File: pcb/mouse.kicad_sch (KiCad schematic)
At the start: 42 parts, among them J1 Conn_02x03_Counter_Clockwise, SW1 SW_MEC_5E, SW2 SW_DPDT_x2, SW3 SW_DPDT_x2, SW4 RotaryEncoder, SW5 SW_DPDT_x2, SW6 SW_DPDT_x2, U1 STM32F042K6Tx, U2 pmw3360-t2qu

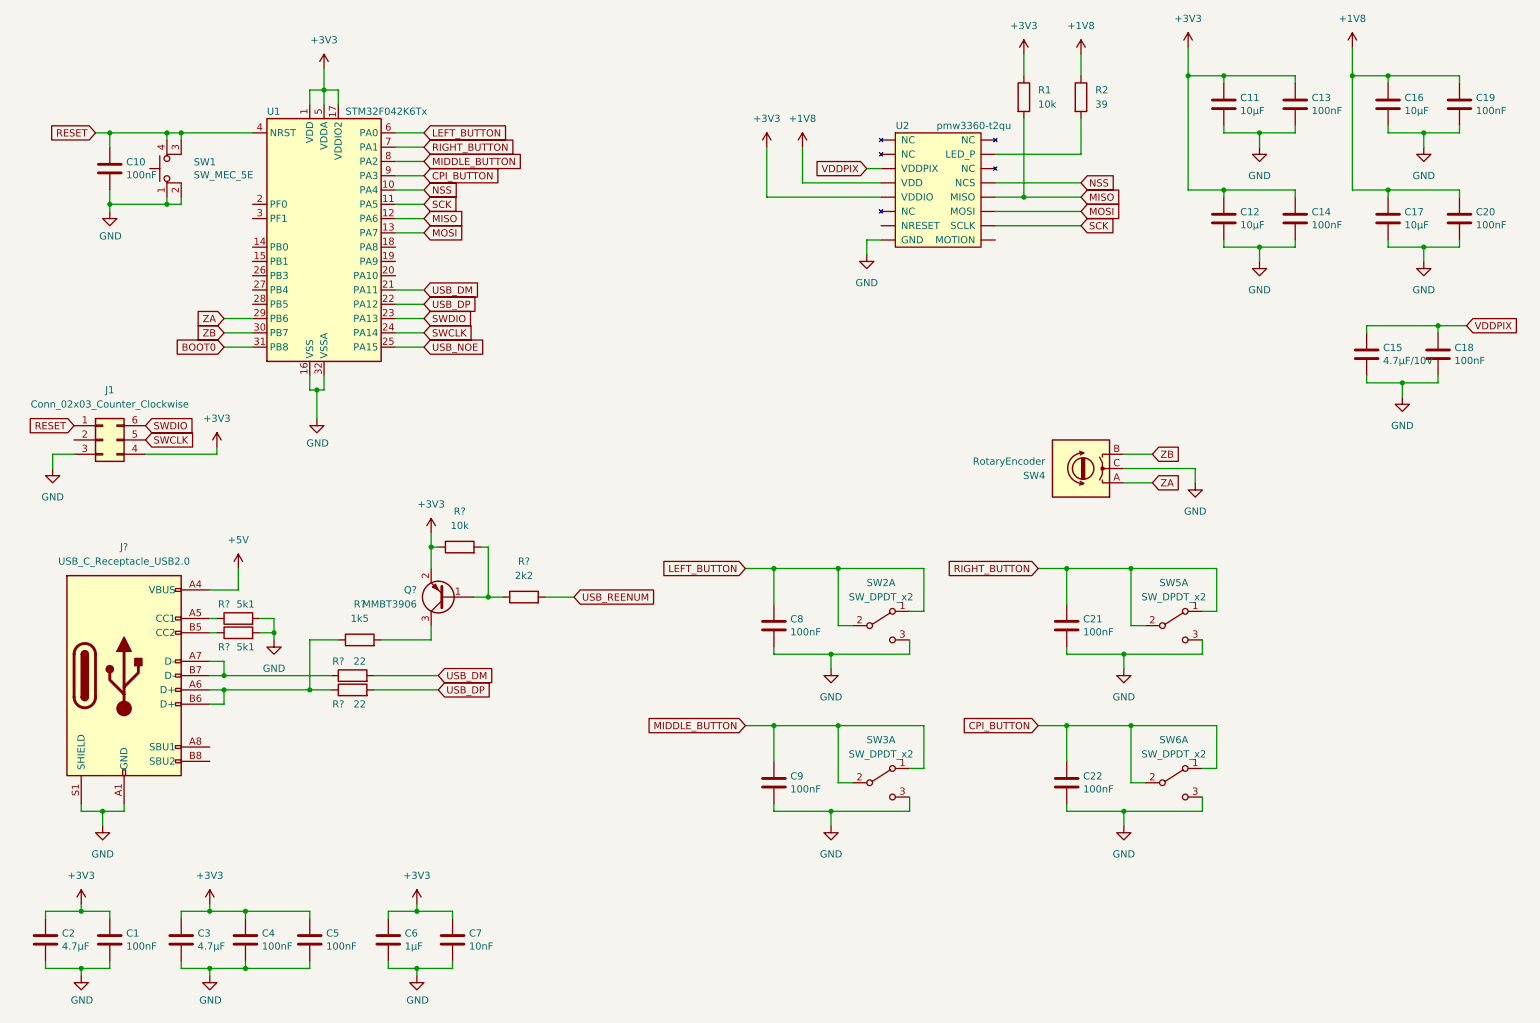
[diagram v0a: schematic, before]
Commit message: - added power input LDOs - broken out schematics to multiple sheets
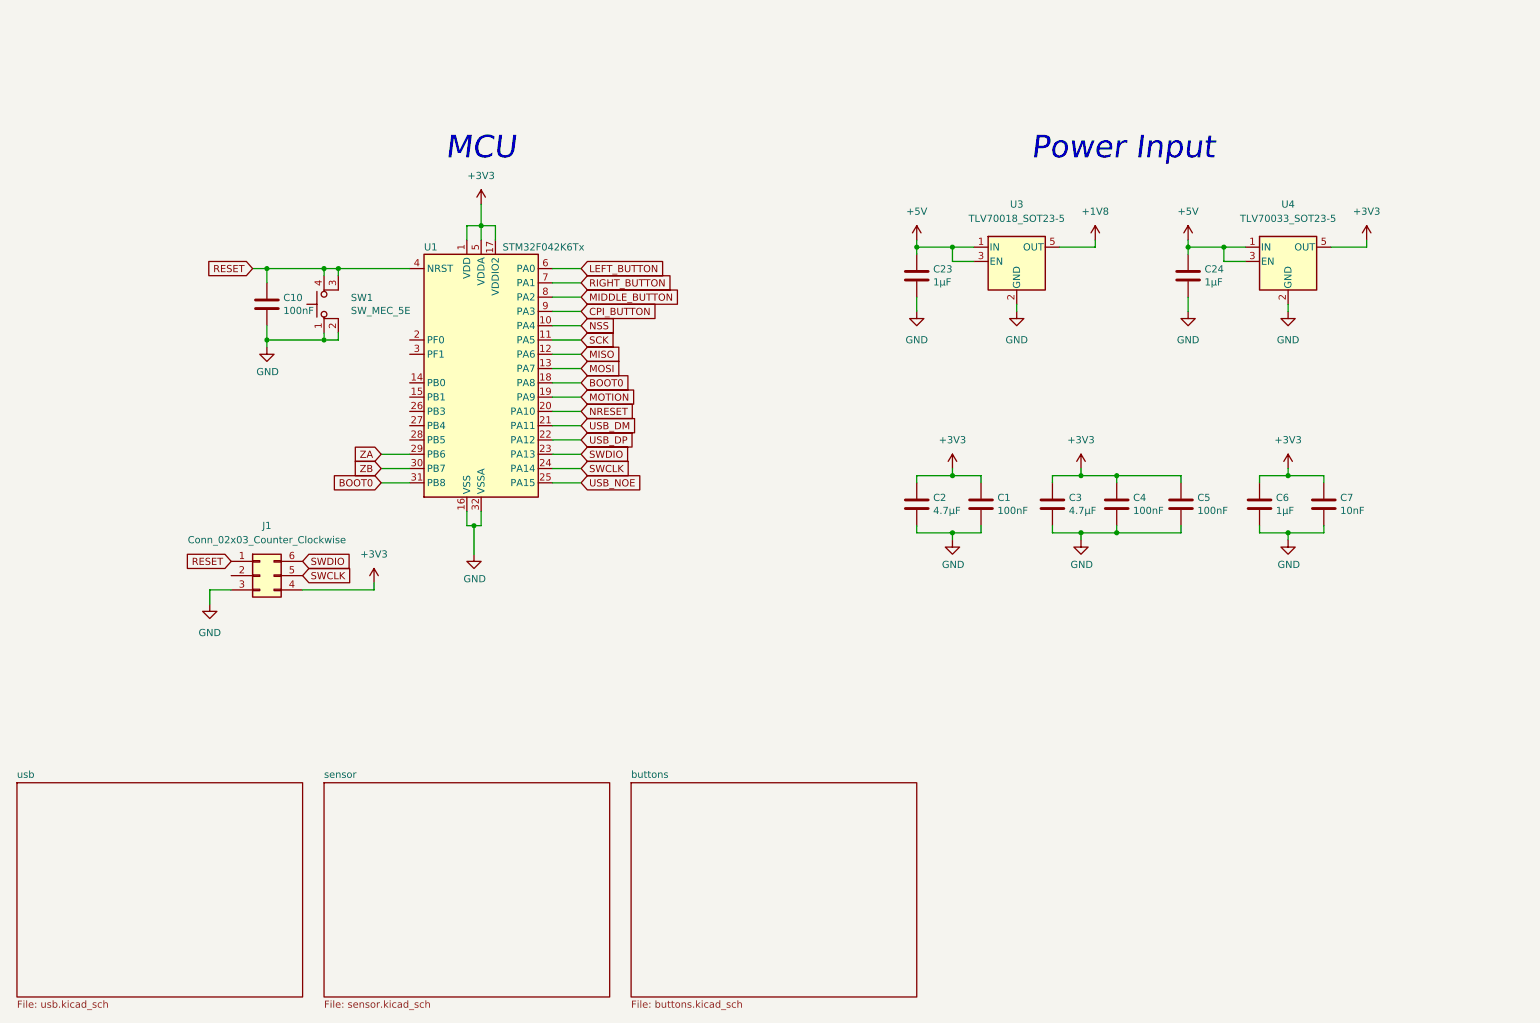
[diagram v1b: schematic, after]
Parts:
- removed C11, C12, C16, C17: 10μF, symbol Device:C
- removed C13, C14, C18, C19, C20, C21, C22, C8, C9: 100nF, symbol Device:C
- removed C15: 4.7μF/10V, symbol Device:C
- removed J?: USB_C_Receptacle_USB2.0, symbol Connector:USB_C_Receptacle_USB2.0
- removed Q?: MMBT3906, Package_TO_SOT_SMD:SOT-23, symbol Transistor_BJT:MMBT3906
- removed R1, R?: 10k, symbol Device:R
- removed R2: 39, symbol Device:R
- removed R? (x2): 22, symbol Device:R
- removed R? (x2): 5k1, symbol Device:R
- removed R?: 1k5, symbol Device:R
- removed R?: 2k2, symbol Device:R
- removed SW2, SW3, SW5, SW6: SW_DPDT_x2, symbol Switch:SW_DPDT_x2
- removed SW4: RotaryEncoder, symbol Device:RotaryEncoder
- removed U2: pmw3360-t2qu, symbol mouse:pmw3360-t2qu
- added C23, C24: 1μF, symbol Device:C
- added U3: TLV70018_SOT23-5, Package_TO_SOT_SMD:SOT-23-5, symbol Regulator_Linear:TLV70018_SOT23-5
- added U4: TLV70033_SOT23-5, Package_TO_SOT_SMD:SOT-23-5, symbol Regulator_Linear:TLV70033_SOT23-5
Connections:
- net +1V8: now also U3.5 (OUT)
- net +3V3: now also U4.5 (OUT)
- net +5V: now also C23.1, C24.1, U3.1 (IN), U3.3 (EN), U4.1 (IN), U4.3 (EN)
- net BOOT0: now also U1.18 (PA8)
- net GND: now also C23.2, C24.2, U3.2 (GND), U4.2 (GND)
- net MOTION: now reaches U1.19 (PA9)
- net NRESET: now reaches U1.20 (PA10)
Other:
- added sheet buttons (buttons.kicad_sch)
- added sheet sensor (sensor.kicad_sch)
- added sheet usb (usb.kicad_sch)
- note added: "MCU"
- note added: "Power Input"
- moved on the sheet: C1, C10, C2, C3, C4, C5, C6, C7, J1, SW1, U1

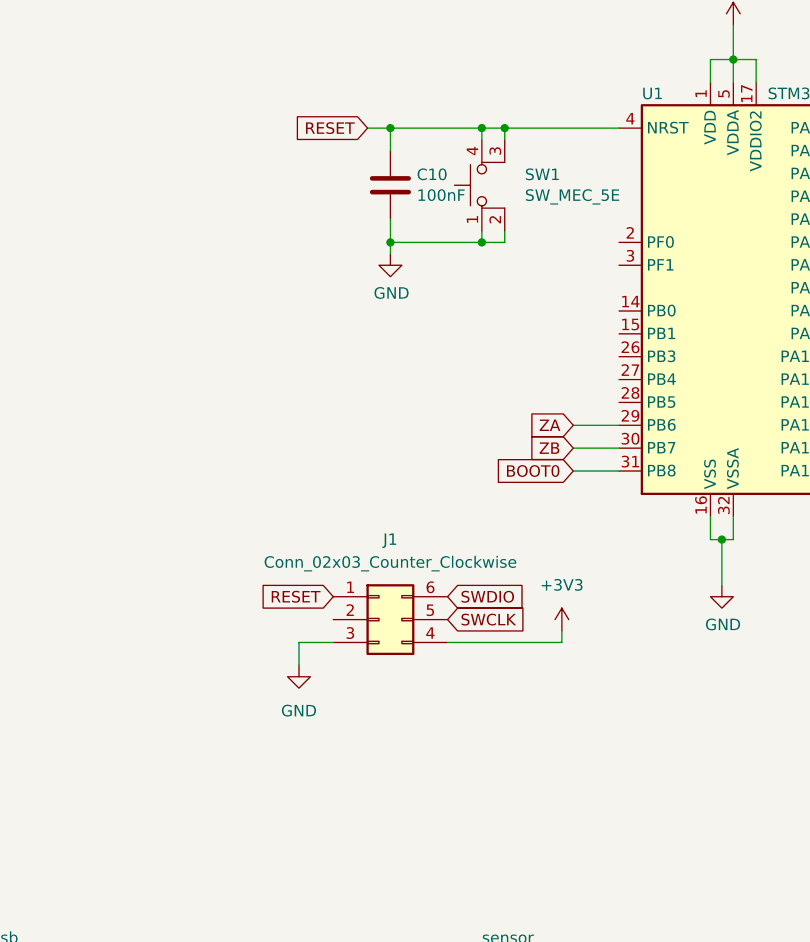
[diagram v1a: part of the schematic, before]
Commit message: cleaned up symbols in schematics a bit
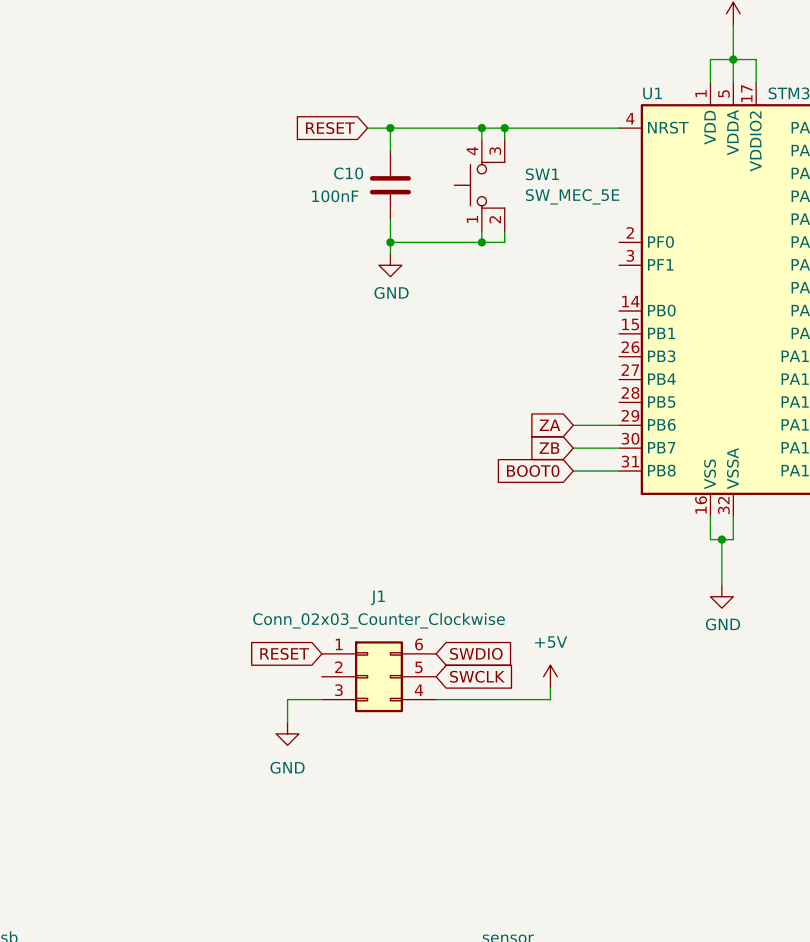
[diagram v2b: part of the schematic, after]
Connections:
- net +3V3: no longer J1.4 (Pin_4)
- net +5V: now also J1.4 (Pin_4)
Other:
- moved on the sheet: J1
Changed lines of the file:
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@@
     (stroke (width 0) (type default) (color 0 0 0 0))
   )
-  (wire (pts (xy 77.47 120.65) (xy 64.77 120.65))
+  (wire (pts (xy 76.2 127) (xy 63.5 127))
     (stroke (width 0) (type default) (color 0 0 0 0))
   )
@@
     (stroke (width 0) (type default) (color 0 0 0 0))
   )
-  (wire (pts (xy 77.47 119.38) (xy 77.47 120.65))
+  (wire (pts (xy 76.2 125.73) (xy 76.2 127))
     (stroke (width 0) (type default) (color 0 0 0 0))
   )
@@
     (stroke (width 0) (type default) (color 0 0 0 0))
   )
-  (wire (pts (xy 48.26 120.65) (xy 48.26 123.19))
+  (wire (pts (xy 46.99 127) (xy 46.99 129.54))
     (stroke (width 0) (type default) (color 0 0 0 0))
   )
@@
     (stroke (width 0) (type default) (color 0 0 0 0))
   )
-  (wire (pts (xy 52.07 120.65) (xy 48.26 120.65))
+  (wire (pts (xy 50.8 127) (xy 46.99 127))
     (stroke (width 0) (type default) (color 0 0 0 0))
   )
@@
     )
   )
-  (global_label "SWCLK" (shape input) (at 64.77 118.11 0) (fields_autoplaced)
-    (effects (font (size 1.27 1.27)) (justify left))
-    (property "Intersheet References" "${INTERSHEET_REFS}" (id 0) (at 73.3232 118.0306 0)
-      (effects (font (size 1.27 1.27)) (justify left) hide)
-    )
-  )
-  (global_label "RESET" (shape input) (at 52.07 115.57 180) (fields_autoplaced)
+  (global_label "SWCLK" (shape input) (at 63.5 124.46 0) (fields_autoplaced)
+    (effects (font (size 1.27 1.27)) (justify left))
+    (property "Intersheet References" "${INTERSHEET_REFS}" (id 0) (at 72.0532 124.3806 0)
+      (effects (font (size 1.27 1.27)) (justify left) hide)
+    )
+  )
+  (global_label "RESET" (shape input) (at 50.8 121.92 180) (fields_autoplaced)
     (effects (font (size 1.27 1.27)) (justify right))
-    (property "Intersheet References" "${INTERSHEET_REFS}" (id 0) (at 44.0006 115.4906 0)
+    (property "Intersheet References" "${INTERSHEET_REFS}" (id 0) (at 42.7306 121.8406 0)
       (effects (font (size 1.27 1.27)) (justify right) hide)
     )
   )
-  (global_label "SWDIO" (shape input) (at 64.77 115.57 0) (fields_autoplaced)
-    (effects (font (size 1.27 1.27)) (justify left))
-    (property "Intersheet References" "${INTERSHEET_REFS}" (id 0) (at 72.9604 115.4906 0)
+  (global_label "SWDIO" (shape input) (at 63.5 121.92 0) (fields_autoplaced)
+    (effects (font (size 1.27 1.27)) (justify left))
+    (property "Intersheet References" "${INTERSHEET_REFS}" (id 0) (at 71.6904 121.8406 0)
       (effects (font (size 1.27 1.27)) (justify left) hide)
     )
@@
   (symbol (lib_id "Device:C") (at 58.42 69.85 0) (unit 1)
     (in_bom yes) (on_board yes)
-    (property "Reference" "C10" (id 0) (at 61.341 68.6816 0)
-      (effects (font (size 1.27 1.27)) (justify left))
-    )
-    (property "Value" "100nF" (id 1) (at 61.341 70.993 0)
+    (property "Reference" "C10" (id 0) (at 52.07 68.58 0)
+      (effects (font (size 1.27 1.27)) (justify left))
+    )
+    (property "Value" "100nF" (id 1) (at 49.53 71.12 0)
       (effects (font (size 1.27 1.27)) (justify left))
     )
@@
     (pin "9")
   )
-  (symbol (lib_id "power:+3V3") (at 77.47 119.38 0) (unit 1)
-    (in_bom yes) (on_board yes) (fields_autoplaced)
-    (property "Reference" "#PWR02" (id 0) (at 77.47 123.19 0)
-      (effects (font (size 1.27 1.27)) hide)
-    )
-    (property "Value" "+3V3" (id 1) (at 77.47 114.3 0))
-    (property "Footprint" "" (id 2) (at 77.47 119.38 0)
-      (effects (font (size 1.27 1.27)) hide)
-    )
-    (property "Datasheet" "" (id 3) (at 77.47 119.38 0)
-      (effects (font (size 1.27 1.27)) hide)
-    )
-    (pin "1")
-  )
   (symbol (lib_id "Device:C") (at 173.99 64.77 0) (unit 1)
     (in_bom yes) (on_board yes)
@@
     (pin "2")
   )
-  (symbol (lib_id "Connector_Generic:Conn_02x03_Counter_Clockwise") (at 57.15 118.11 0) (unit 1)
-    (in_bom yes) (on_board yes)
-    (property "Reference" "J1" (id 0) (at 58.42 109.22 0))
-    (property "Value" "Conn_02x03_Counter_Clockwise" (id 1) (at 58.42 111.76 0))
-    (property "Footprint" "" (id 2) (at 57.15 118.11 0)
-      (effects (font (size 1.27 1.27)) hide)
-    )
-    (property "Datasheet" "~" (id 3) (at 57.15 118.11 0)
+  (symbol (lib_id "Connector_Generic:Conn_02x03_Counter_Clockwise") (at 55.88 124.46 0) (unit 1)
+    (in_bom yes) (on_board yes)
+    (property "Reference" "J1" (id 0) (at 57.15 115.57 0))
+    (property "Value" "Conn_02x03_Counter_Clockwise" (id 1) (at 57.15 118.11 0))
+    (property "Footprint" "" (id 2) (at 55.88 124.46 0)
+      (effects (font (size 1.27 1.27)) hide)
+    )
+    (property "Datasheet" "~" (id 3) (at 55.88 124.46 0)
       (effects (font (size 1.27 1.27)) hide)
     )
@@
     (pin "2")
   )
-  (symbol (lib_id "power:GND") (at 48.26 123.19 0) (unit 1)
-    (in_bom yes) (on_board yes) (fields_autoplaced)
-    (property "Reference" "#PWR01" (id 0) (at 48.26 129.54 0)
-      (effects (font (size 1.27 1.27)) hide)
-    )
-    (property "Value" "GND" (id 1) (at 48.26 128.27 0))
-    (property "Footprint" "" (id 2) (at 48.26 123.19 0)
-      (effects (font (size 1.27 1.27)) hide)
-    )
-    (property "Datasheet" "" (id 3) (at 48.26 123.19 0)
+  (symbol (lib_id "power:GND") (at 46.99 129.54 0) (unit 1)
+    (in_bom yes) (on_board yes) (fields_autoplaced)
+    (property "Reference" "#PWR01" (id 0) (at 46.99 135.89 0)
+      (effects (font (size 1.27 1.27)) hide)
+    )
+    (property "Value" "GND" (id 1) (at 46.99 134.62 0))
+    (property "Footprint" "" (id 2) (at 46.99 129.54 0)
+      (effects (font (size 1.27 1.27)) hide)
+    )
+    (property "Datasheet" "" (id 3) (at 46.99 129.54 0)
       (effects (font (size 1.27 1.27)) hide)
     )
@@
     )
     (property "Datasheet" "" (id 3) (at 173.99 71.12 0)
+      (effects (font (size 1.27 1.27)) hide)
+    )
+    (pin "1")
+  )
+  (symbol (lib_id "power:+5V") (at 76.2 125.73 0) (unit 1)
+    (in_bom yes) (on_board yes) (fields_autoplaced)
+    (property "Reference" "#PWR?" (id 0) (at 76.2 129.54 0)
+      (effects (font (size 1.27 1.27)) hide)
+    )
+    (property "Value" "+5V" (id 1) (at 76.2 120.65 0))
+    (property "Footprint" "" (id 2) (at 76.2 125.73 0)
+      (effects (font (size 1.27 1.27)) hide)
+    )
+    (property "Datasheet" "" (id 3) (at 76.2 125.73 0)
       (effects (font (size 1.27 1.27)) hide)
     )
@@
       (reference "#PWR01") (unit 1) (value "GND") (footprint "")
     )
-    (path "/264a1897-22dc-4b50-bce5-2c0b11f540af"
-      (reference "#PWR02") (unit 1) (value "+3V3") (footprint "")
-    )
     (path "/ae55bc0a-c1c2-4f8c-b0c4-7c93c846017b"
       (reference "#PWR03") (unit 1) (value "+3V3") (footprint "")
@@
       (reference "#PWR0109") (unit 1) (value "GND") (footprint "")
     )
+    (path "/d766d23a-9097-47c7-a060-c09ab0604957"
+      (reference "#PWR?") (unit 1) (value "+5V") (footprint "")
+    )
     (path "/00000000-0000-0000-0000-000061cd3bd9"
       (reference "C1") (unit 1) (value "100nF") (footprint "")
@@
     )
     (path "/2bfe00f4-e0c8-4774-8d9e-4d480f9c91ad/6c8dcf43-11bc-40e7-86d9-2a681e8f1407"
-      (reference "U2") (unit 1) (value "pmw3360-t2qu") (footprint "")
+      (reference "U2") (unit 1) (value "pmw3360-t2qu") (footprint "mouse:pmw3360-t2qu")
     )
     (path "/9b1c21d6-1353-4fb6-9323-f943e2468fdd"
